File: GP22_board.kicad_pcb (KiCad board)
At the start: 4 copper layers, 100 x 100 mm, 145 parts, among them CON1 5V power input, IC1 ATMEGA328P-A, P1 TTLOut1, P10 S- DC/AC, P11 S+ DC/AC, P12 S- DC/AC, P13 TTLOut2, P14 TTLOut3, P15 PWR_SEL, P16 FILT_SEL, P2 SineInput, P3 TTLInput, P4 USB_OTG, P5 ICSP, P6 STInput, P7 S+ DC/AC, P8 S- DC/AC, P9 S+ DC/AC, SW1 START, SW2 STOP1, SW3 STOP2, U1 RS 252-210, U10 XC6206, U11 ISO7242, U12 FT232RL, U2 GP22, U3 LTC6957-4, U4 ISO3088, U5 IDT49FCT, U6 LD1117S33TR, U7 MC74VHC1GT04, U8 SN74LV8154, U9 SC74HC165N, X1 TSX-3225 X1E0000210013, Y1 4MHz, Y2 32.768 kHz

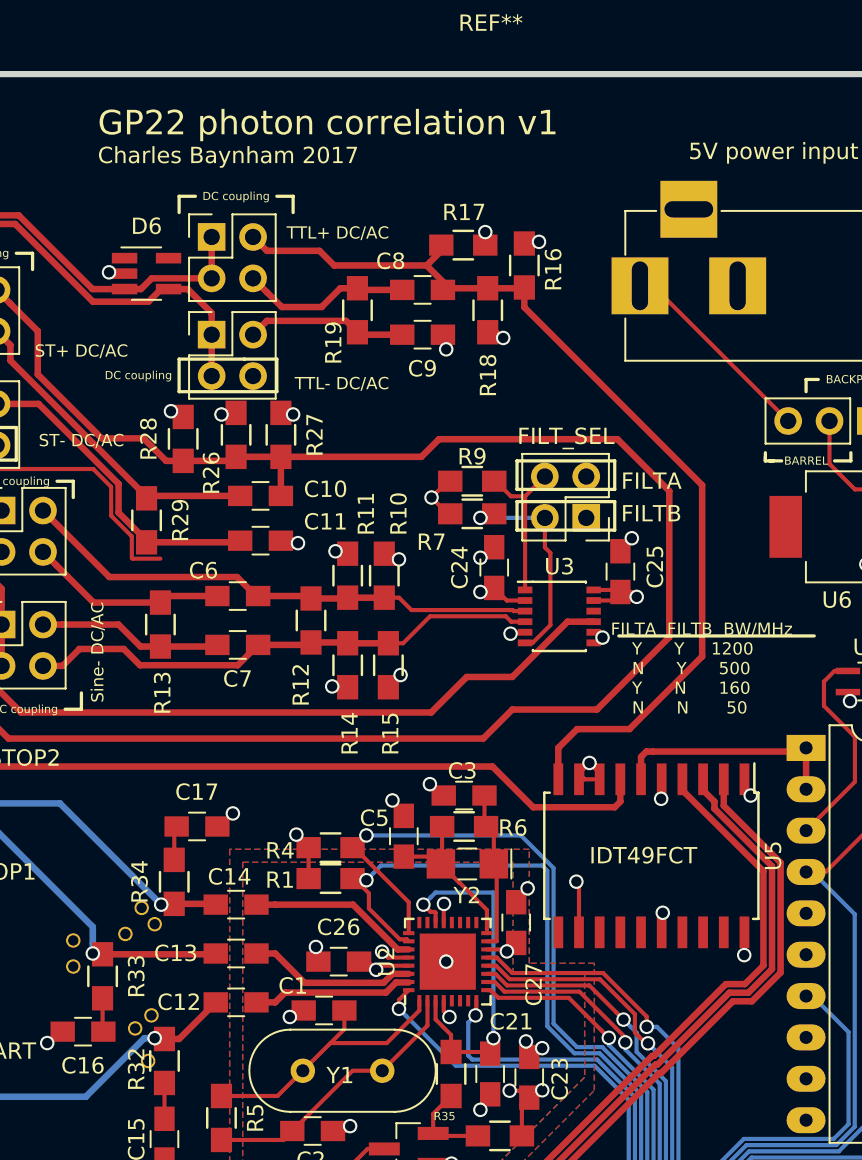
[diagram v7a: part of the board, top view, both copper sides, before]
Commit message: Bug fix: CS for TDC was floating to undefined level when MC was not flashed, causing SPI pollution
Added a 10k pullup resistor to CS to fix this
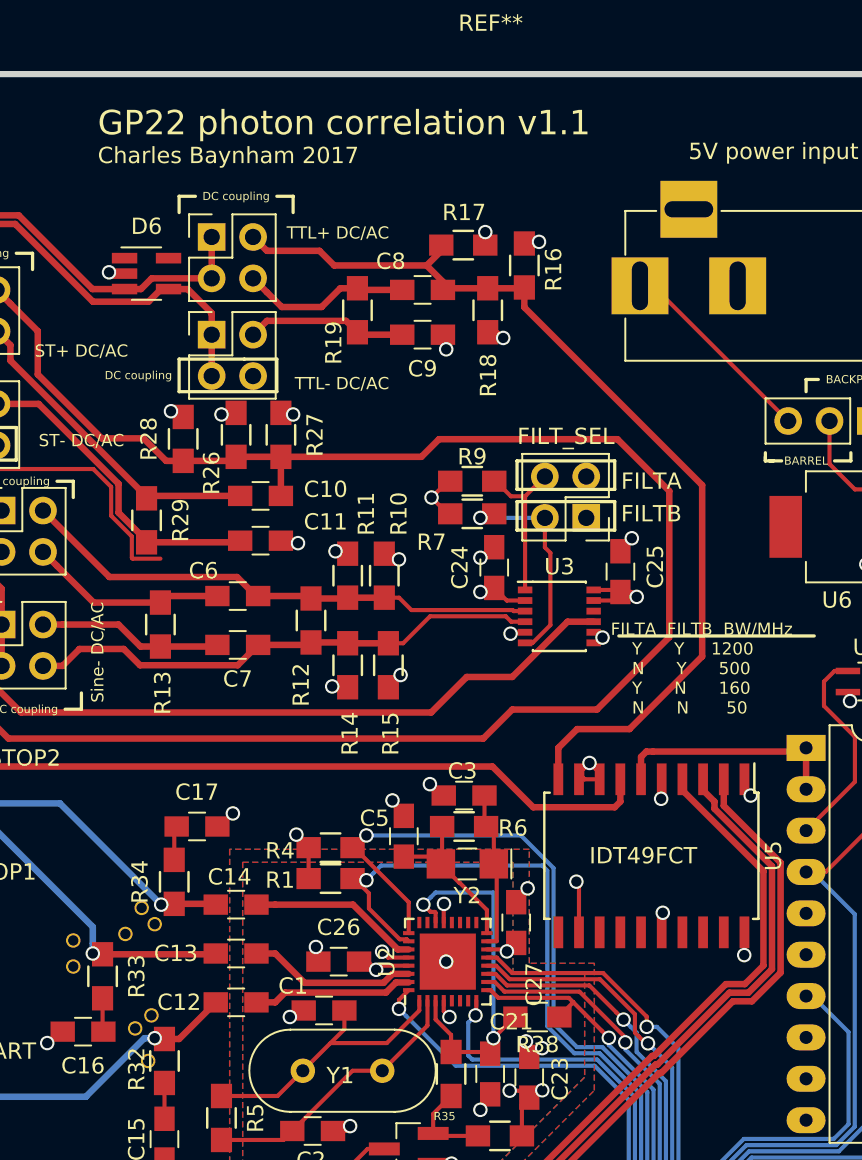
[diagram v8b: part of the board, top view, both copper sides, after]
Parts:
- added R38: 10k, Resistors_SMD:R_0805_HandSoldering, F.Cu at (214.5, 92.9)
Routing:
- net /GP22_VIO: track 22.4 -> 24.3 mm
- net /GP22_CS: track 46.5 -> 47.7 mm
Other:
- board text added: "GP22 photon correlation v1.1"
- board text removed: "GP22 photon correlation v1"
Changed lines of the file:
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@@
 (kicad_pcb (version 4) (host pcbnew 4.0.4-stable)
   (general
-    (links 402)
+    (links 404)
     (no_connects 14)
     (area 24.5 19.5 276.000001 160.625)
     (thickness 1.6)
     (drawings 81)
-    (tracks 1405)
+    (tracks 1410)
     (zones 0)
-    (modules 145)
+    (modules 146)
     (nets 110)
   )
@@
       (net 32 GND) (zone_connect 2))
   )
+  (module Resistors_SMD:R_0805_HandSoldering (layer F.Cu)
+    (at 214.5 92.9 180)
+    (descr "Resistor SMD 0805, hand soldering")
+    (tags "resistor 0805")
+    (attr smd)
+    (fp_text reference R38 (at 0 -1.7 180) (layer F.SilkS)
+      (effects (font (size 1 1) (thickness 0.15)))
+    )
+    (fp_text value 10k (at 0 1.75 180) (layer F.Fab)
+      (effects (font (size 1 1) (thickness 0.15)))
+    )
+    (fp_text user %R (at 0 -1.7 180) (layer F.Fab)
+      (effects (font (size 1 1) (thickness 0.15)))
+    )
+    (fp_line (start -1 0.62) (end -1 -0.62) (layer F.Fab) (width 0.1))
+    (fp_line (start 1 0.62) (end -1 0.62) (layer F.Fab) (width 0.1))
+    (fp_line (start 1 -0.62) (end 1 0.62) (layer F.Fab) (width 0.1))
+    (fp_line (start -1 -0.62) (end 1 -0.62) (layer F.Fab) (width 0.1))
+    (fp_line (start 0.6 0.88) (end -0.6 0.88) (layer F.SilkS) (width 0.12))
+    (fp_line (start -0.6 -0.88) (end 0.6 -0.88) (layer F.SilkS) (width 0.12))
+    (fp_line (start -2.35 -0.9) (end 2.35 -0.9) (layer F.CrtYd) (width 0.05))
+    (fp_line (start -2.35 -0.9) (end -2.35 0.9) (layer F.CrtYd) (width 0.05))
+    (fp_line (start 2.35 0.9) (end 2.35 -0.9) (layer F.CrtYd) (width 0.05))
+    (fp_line (start 2.35 0.9) (end -2.35 0.9) (layer F.CrtYd) (width 0.05))
+    (pad 1 smd rect (at -1.35 0 180) (size 1.5 1.3) (layers F.Cu F.Paste F.Mask)
+      (net 58 /GP22_CS))
+    (pad 2 smd rect (at 1.35 0 180) (size 1.5 1.3) (layers F.Cu F.Paste F.Mask)
+      (net 52 /GP22_VIO))
+    (model Resistors_SMD.3dshapes/R_0805.wrl
+      (at (xyz 0 0 0))
+      (scale (xyz 1 1 1))
+      (rotate (xyz 0 0 0))
+    )
+  )
   (gr_text "Charles Baynham 2017" (at 187.5 40) (layer F.SilkS)
     (effects (font (size 1 1) (thickness 0.25)) (justify left))
@@
     (effects (font (size 0.75 0.75) (thickness 0.1875)))
   )
-  (gr_text "GP22 photon correlation v1" (at 187.5 38) (layer F.SilkS)
+  (gr_text "GP22 photon correlation v1.1" (at 187.5 38) (layer F.SilkS)
     (effects (font (size 1.5 1.5) (thickness 0.3)) (justify left))
   )
@@
   (via (at 234.3 113.8) (size 0.889) (drill 0.635) (layers F.Cu B.Cu) (net 51))
   (segment (start 234.245 113.855) (end 234.3 113.8) (width 0.254) (layer F.Cu) (net 51))
+  (segment (start 213.15 92.9) (end 213.1 92.9) (width 0.254) (layer F.Cu) (net 52))
+  (segment (start 213.1 92.9) (end 211.8 94.2) (width 0.254) (layer F.Cu) (net 52))
   (segment (start 211.8 94.2) (end 211.8 85.256054) (width 0.254) (layer B.Cu) (net 52))
   (segment (start 211.8 85.256054) (end 208.243946 85.256054) (width 0.254) (layer B.Cu) (net 52))
@@
   (segment (start 217.701232 124.1) (end 219.222664 122.578568) (width 0.254) (layer F.Cu) (net 57))
   (via (at 219.222664 122.095558) (size 0.889) (drill 0.635) (layers F.Cu B.Cu) (net 57))
+  (segment (start 215.85 92.9) (end 215.85 92.85) (width 0.254) (layer F.Cu) (net 58))
+  (segment (start 215.85 92.85) (end 216.704275 91.995725) (width 0.254) (layer F.Cu) (net 58))
   (segment (start 213.4 119.45) (end 213.4 121.6) (width 0.254) (layer F.Cu) (net 58))
   (segment (start 213.4 121.6) (end 214.3 122.5) (width 0.254) (layer F.Cu) (net 58))
@@
   (segment (start 211.625 91.25) (end 212.099044 91.724044) (width 0.254) (layer F.Cu) (net 58))
   (via (at 218.887194 94.178644) (size 0.889) (drill 0.635) (layers F.Cu B.Cu) (net 58))
-  (segment (start 216.432594 91.724044) (end 218.442695 93.734145) (width 0.254) (layer F.Cu) (net 58))
+  (segment (start 216.432594 91.724044) (end 216.704275 91.995725) (width 0.254) (layer F.Cu) (net 58))
+  (segment (start 216.704275 91.995725) (end 218.442695 93.734145) (width 0.254) (layer F.Cu) (net 58))
   (segment (start 212.099044 91.724044) (end 216.432594 91.724044) (width 0.254) (layer F.Cu) (net 58))
   (segment (start 211.4 91.25) (end 211.625 91.25) (width 0.254) (layer F.Cu) (net 58))
